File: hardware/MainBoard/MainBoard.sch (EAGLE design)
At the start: 220 parts, among them J1 CON-71741-2184-BOT, J2 CON-71741-2184-TOP, J3 CON-FTSH-105-01-L-DV-K, J4 CON-ZX62R-B-5P, J5 CON-SMA, J6 CON-SMA, J7 CON-RJ45-J0G-0007NL, J8 SWITCH-CJS-1200-1200, M1 MOUNT-HOLE3.3, M2 MOUNT-HOLE3.3, M3 MOUNT-HOLE3.3, M4 MOUNT-HOLE3.3, M5 FIDUCIAL1X2, M6 FIDUCIAL1X2, M7 FIDUCIAL1X2, M8 FIDUCIAL1X2, Q1 MMBT3904, SW1 SWITCH-KSC-201J, SW2 SWITCH-KSC-201J, U1 A2F500M3G-FG256, U2 MAX19706-T4877-4, U3 MAX19706-T4877-4, U4 USBLC6-2SC6, U5 FT232HL, U6 DP83848C-VBH48A, U7 93LC56BT-OT, U8 DS1818-10-SOT-23, U9 LMV112, X1 FOX924B, X2 ECX-31B, X3 ASEM1-C, X5 ECX-42-120

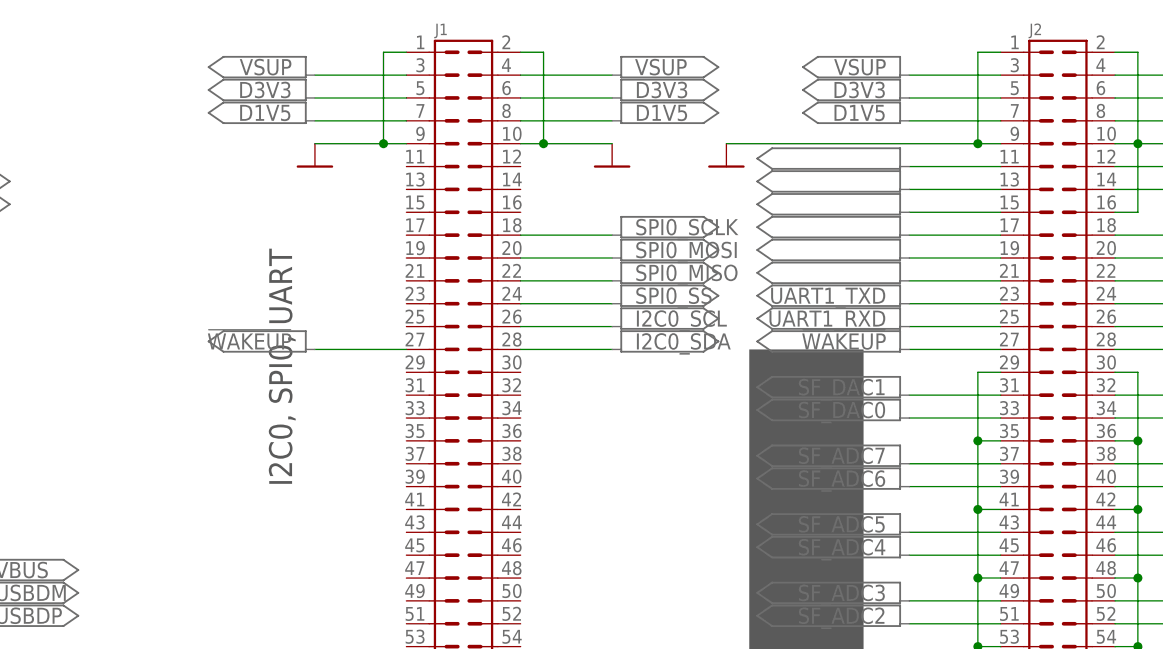
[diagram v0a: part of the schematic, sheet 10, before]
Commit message: Minor updates on the connector on the schematic.
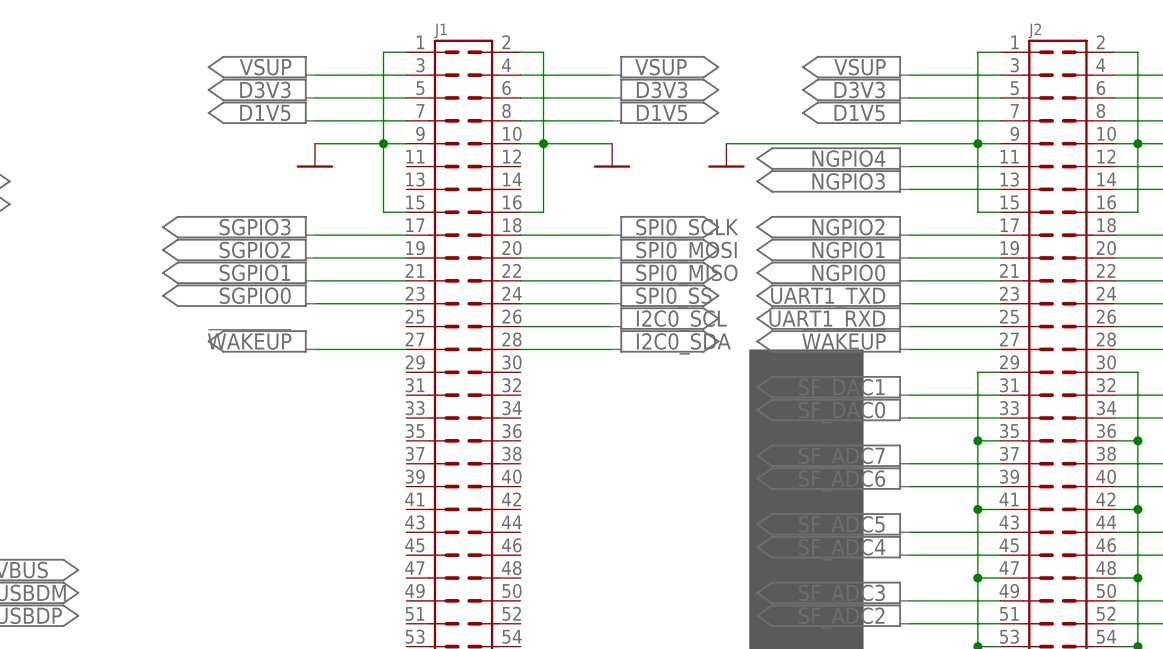
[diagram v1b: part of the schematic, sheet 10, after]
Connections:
- net N$10 renamed NGPIO4
- net N$2 renamed NGPIO3
- net N$3 renamed NGPIO0
- net N$5 renamed NGPIO1
- net N$7 renamed NGPIO2
- removed net N$1: J2.15
- new net SGPIO0: J1.23
- new net SGPIO1: J1.21
- new net SGPIO2: J1.19
- new net SGPIO3: J1.17
- net DGND: now also J1.15, J1.16, J2.15
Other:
- note added: "Make it a differential FPGAIO"
- note removed: "I2C0, SPI0, UART"
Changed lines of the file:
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@@
 <setting verticaltext="up"/>
 </settings>
-<grid distance="0.1" unitdist="inch" unit="inch" style="lines" multiple="1" display="no" altdistance="0.01" altunitdist="inch" altunit="inch"/>
+<grid distance="0.1" unitdist="inch" unit="inch" style="lines" multiple="1" display="no" altdistance="0.05" altunitdist="inch" altunit="inch"/>
 <layers>
 <layer number="1" name="Top" color="4" fill="1" visible="no" active="no"/>
@@
 <layer number="113" name="Route13" color="7" fill="1" visible="no" active="no"/>
 <layer number="114" name="FIXED_SF_PIN" color="2" fill="3" visible="yes" active="yes"/>
-<layer number="116" name="Patch_BOT" color="9" fill="4" visible="yes" active="yes"/>
+<layer number="116" name="Patch_BOT" color="9" fill="4" visible="no" active="yes"/>
 <layer number="117" name="mPads" color="7" fill="1" visible="no" active="no"/>
 <layer number="118" name="mVias" color="7" fill="1" visible="no" active="no"/>
@@
 <part name="PORT350" library="MainBoard" deviceset="PORT7" device=""/>
 <part name="U$20" library="MainBoard" deviceset="DGND" device=""/>
+<part name="PORT323" library="MainBoard" deviceset="PORT7" device=""/>
+<part name="PORT351" library="MainBoard" deviceset="PORT7" device=""/>
+<part name="PORT352" library="MainBoard" deviceset="PORT7" device=""/>
 </parts>
 <sheets>
@@
 <text x="64.77" y="149.86" size="1.778" layer="97">NC</text>
 <text x="45.72" y="76.2" size="50.8" layer="208">CON</text>
-<text x="116.84" y="114.3" size="2.54" layer="97" rot="R90">I2C0, SPI0, UART</text>
-<rectangle x1="167.64" y1="137.16" x2="187.96" y2="151.13" layer="98"/>
+<rectangle x1="170.18" y1="147.32" x2="187.96" y2="152.4" layer="98"/>
+<text x="172.72" y="149.86" size="1.778" layer="98" rot="R90">Make it a differential FPGAIO</text>
 </plain>
 <instances>
@@
 <instance part="PORT346" gate="G$1" x="170.18" y="139.7" rot="MR0"/>
 <instance part="PORT347" gate="G$1" x="170.18" y="142.24" rot="MR0"/>
-<instance part="PORT348" gate="G$1" x="170.18" y="144.78" rot="MR0"/>
+<instance part="PORT348" gate="G$1" x="104.14" y="142.24" rot="MR0"/>
 <instance part="PORT349" gate="G$1" x="170.18" y="147.32" rot="MR0"/>
 <instance part="PORT350" gate="G$1" x="170.18" y="149.86" rot="MR0"/>
+<instance part="PORT323" gate="G$1" x="104.14" y="134.62" rot="MR0"/>
+<instance part="PORT351" gate="G$1" x="104.14" y="137.16" rot="MR0"/>
+<instance part="PORT352" gate="G$1" x="104.14" y="139.7" rot="MR0"/>
 </instances>
 <busses>
@@
 <wire x1="127" y1="152.4" x2="129.54" y2="152.4" width="0.1524" layer="91"/>
 <junction x="127" y="152.4"/>
+<wire x1="127" y1="152.4" x2="127" y2="144.78" width="0.1524" layer="91"/>
+<pinref part="J1" gate="G$1" pin="15"/>
+<wire x1="127" y1="144.78" x2="129.54" y2="144.78" width="0.1524" layer="91"/>
 </segment>
 <segment>
@@
 <wire x1="142.24" y1="152.4" x2="144.78" y2="152.4" width="0.1524" layer="91"/>
 <junction x="144.78" y="152.4"/>
+<pinref part="J1" gate="G$1" pin="16"/>
+<wire x1="142.24" y1="144.78" x2="144.78" y2="144.78" width="0.1524" layer="91"/>
+<wire x1="144.78" y1="144.78" x2="144.78" y2="152.4" width="0.1524" layer="91"/>
 </segment>
 <segment>
@@
 <wire x1="193.04" y1="162.56" x2="195.58" y2="162.56" width="0.1524" layer="91"/>
 <junction x="193.04" y="152.4"/>
+<pinref part="J2" gate="G$1" pin="15"/>
+<wire x1="195.58" y1="144.78" x2="193.04" y2="144.78" width="0.1524" layer="91"/>
+<wire x1="193.04" y1="144.78" x2="193.04" y2="152.4" width="0.1524" layer="91"/>
 </segment>
 <segment>
@@
 </segment>
 </net>
-<net name="N$3" class="0">
+<net name="NGPIO0" class="0">
 <segment>
 <pinref part="J2" gate="G$1" pin="21"/>
 <wire x1="195.58" y1="137.16" x2="185.42" y2="137.16" width="0.1524" layer="91"/>
+<label x="182.88" y="137.16" size="1.778" layer="95" rot="MR0"/>
 </segment>
 </net>
-<net name="N$5" class="0">
+<net name="NGPIO1" class="0">
 <segment>
 <pinref part="J2" gate="G$1" pin="19"/>
 <wire x1="195.58" y1="139.7" x2="185.42" y2="139.7" width="0.1524" layer="91"/>
+<label x="182.88" y="139.7" size="1.778" layer="95" rot="MR0"/>
 </segment>
 </net>
-<net name="N$7" class="0">
+<net name="NGPIO2" class="0">
 <segment>
 <pinref part="J2" gate="G$1" pin="17"/>
 <wire x1="195.58" y1="142.24" x2="185.42" y2="142.24" width="0.1524" layer="91"/>
+<label x="182.88" y="142.24" size="1.778" layer="95" rot="MR0"/>
 </segment>
 </net>
-<net name="N$1" class="0">
+<net name="SGPIO3" class="0">
 <segment>
-<pinref part="J2" gate="G$1" pin="15"/>
-<wire x1="195.58" y1="144.78" x2="185.42" y2="144.78" width="0.1524" layer="91"/>
+<wire x1="129.54" y1="142.24" x2="119.38" y2="142.24" width="0.1524" layer="91"/>
+<label x="116.84" y="142.24" size="1.778" layer="95" rot="MR0"/>
+<pinref part="J1" gate="G$1" pin="17"/>
 </segment>
 </net>
-<net name="N$2" class="0">
+<net name="NGPIO3" class="0">
 <segment>
 <pinref part="J2" gate="G$1" pin="13"/>
 <wire x1="195.58" y1="147.32" x2="185.42" y2="147.32" width="0.1524" layer="91"/>
+<label x="182.88" y="147.32" size="1.778" layer="95" rot="MR0"/>
 </segment>
 </net>
-<net name="N$10" class="0">
+<net name="NGPIO4" class="0">
 <segment>
 <pinref part="J2" gate="G$1" pin="11"/>
 <wire x1="195.58" y1="149.86" x2="185.42" y2="149.86" width="0.1524" layer="91"/>
+<label x="182.88" y="149.86" size="1.778" layer="95" rot="MR0"/>
 </segment>
 </net>
@@
 </segment>
 </net>
+<net name="SGPIO0" class="0">
+<segment>
+<pinref part="J1" gate="G$1" pin="23"/>
+<wire x1="129.54" y1="134.62" x2="119.38" y2="134.62" width="0.1524" layer="91"/>
+<label x="116.84" y="134.62" size="1.778" layer="95" rot="MR0"/>
+</segment>
+</net>
+<net name="SGPIO1" class="0">
+<segment>
+<pinref part="J1" gate="G$1" pin="21"/>
+<wire x1="129.54" y1="137.16" x2="119.38" y2="137.16" width="0.1524" layer="91"/>
+<label x="116.84" y="137.16" size="1.778" layer="95" rot="MR0"/>
+</segment>
+</net>
+<net name="SGPIO2" class="0">
+<segment>
+<pinref part="J1" gate="G$1" pin="19"/>
+<wire x1="129.54" y1="139.7" x2="119.38" y2="139.7" width="0.1524" layer="91"/>
+<label x="116.84" y="139.7" size="1.778" layer="95" rot="MR0"/>
+</segment>
+</net>

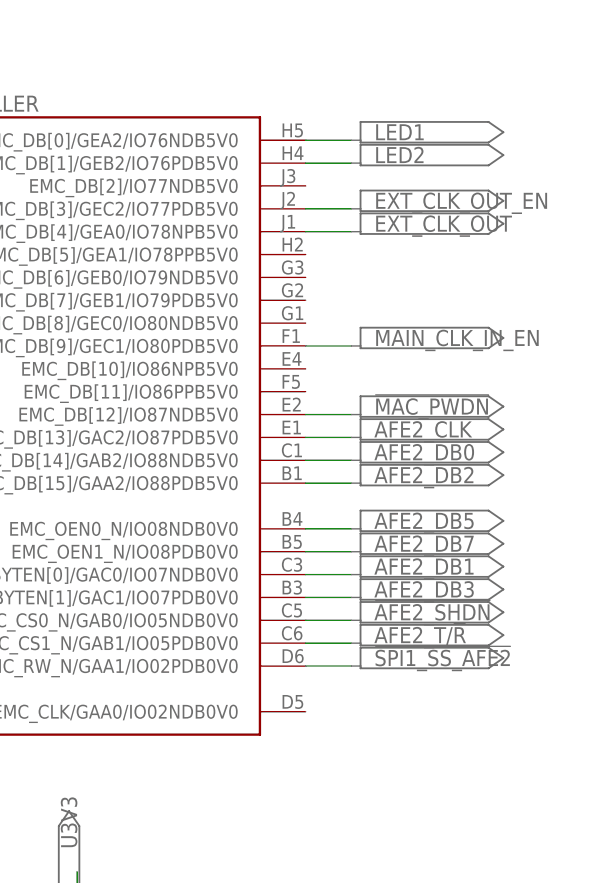
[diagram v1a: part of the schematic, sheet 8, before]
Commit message: 
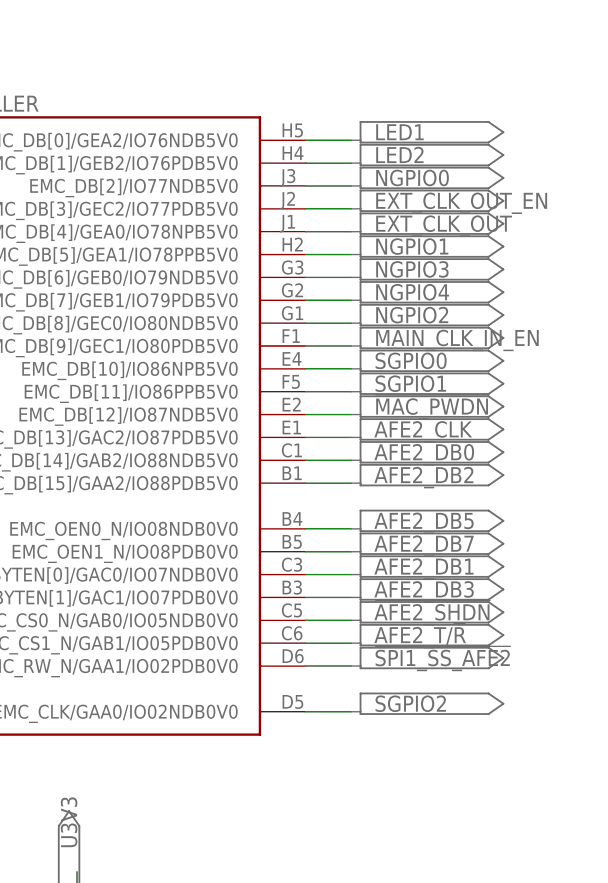
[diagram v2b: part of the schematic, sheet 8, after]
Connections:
- removed net N$6: U1-IOB.IO84NDB5V0
- net NGPIO0: now also U1-EXTERNAL-MEMORY-CONTROLLER.EMC_DB[2]/IO77NDB5V0
- net NGPIO1: now also U1-EXTERNAL-MEMORY-CONTROLLER.EMC_DB[5]/GEA1/IO78PPB5V0
- net NGPIO2: now also U1-EXTERNAL-MEMORY-CONTROLLER.EMC_DB[8]/GEC0/IO80NDB5V0
- net NGPIO3: now also U1-EXTERNAL-MEMORY-CONTROLLER.EMC_DB[6]/GEB0/IO79NDB5V0
- net NGPIO4: now also U1-EXTERNAL-MEMORY-CONTROLLER.EMC_DB[7]/GEB1/IO79PDB5V0
- net SGPIO0: now also U1-EXTERNAL-MEMORY-CONTROLLER.EMC_DB[10]/IO86NPB5V0
- net SGPIO1: now also U1-EXTERNAL-MEMORY-CONTROLLER.EMC_DB[11]/IO86PPB5V0
- net SGPIO2: now also U1-EXTERNAL-MEMORY-CONTROLLER.EMC_CLK/GAA0/IO02NDB0V0
- net SGPIO3: now also U1-IOB.IO84NDB5V0
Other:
- note added: "Make it a differential GCL IN"
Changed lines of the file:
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@@
 <layer number="113" name="Route13" color="7" fill="1" visible="no" active="no"/>
 <layer number="114" name="FIXED_SF_PIN" color="2" fill="3" visible="yes" active="yes"/>
-<layer number="116" name="Patch_BOT" color="9" fill="4" visible="no" active="yes"/>
+<layer number="116" name="Patch_BOT" color="9" fill="4" visible="yes" active="yes"/>
 <layer number="117" name="mPads" color="7" fill="1" visible="no" active="no"/>
 <layer number="118" name="mVias" color="7" fill="1" visible="no" active="no"/>
@@
 <part name="PORT351" library="MainBoard" deviceset="PORT7" device=""/>
 <part name="PORT352" library="MainBoard" deviceset="PORT7" device=""/>
+<part name="PORT353" library="MainBoard" deviceset="PORT7" device=""/>
+<part name="PORT354" library="MainBoard" deviceset="PORT7" device=""/>
+<part name="PORT355" library="MainBoard" deviceset="PORT7" device=""/>
+<part name="PORT356" library="MainBoard" deviceset="PORT7" device=""/>
+<part name="PORT357" library="MainBoard" deviceset="PORT7" device=""/>
+<part name="PORT358" library="MainBoard" deviceset="PORT7" device=""/>
+<part name="PORT359" library="MainBoard" deviceset="PORT7" device=""/>
+<part name="PORT360" library="MainBoard" deviceset="PORT7" device=""/>
 </parts>
 <sheets>
@@
 <plain>
 <text x="198.12" y="20.32" size="5.08" layer="97">USB</text>
-<rectangle x1="218.44" y1="86.36" x2="238.76" y2="99.06" layer="98"/>
 <rectangle x1="114.3" y1="88.9" x2="134.62" y2="96.52" layer="98"/>
 <text x="167.64" y="38.1" size="2.54" layer="97">EEPROM</text>
@@
 <rectangle x1="109.22" y1="111.76" x2="116.84" y2="116.84" layer="101"/>
 <rectangle x1="76.2" y1="109.22" x2="104.14" y2="160.02" layer="116"/>
+<rectangle x1="218.44" y1="149.86" x2="238.76" y2="151.13" layer="116"/>
+<rectangle x1="218.44" y1="134.62" x2="238.76" y2="144.78" layer="116"/>
+<rectangle x1="220.98" y1="127" x2="238.76" y2="132.08" layer="116"/>
+<rectangle x1="218.44" y1="91.44" x2="238.76" y2="93.98" layer="116"/>
 </plain>
 <instances>
@@
 <instance part="PORT299" gate="G$1" x="236.22" y="144.78"/>
 <instance part="PORT300" gate="G$1" x="236.22" y="147.32"/>
+<instance part="PORT353" gate="G$1" x="236.22" y="142.24"/>
+<instance part="PORT354" gate="G$1" x="236.22" y="139.7"/>
+<instance part="PORT355" gate="G$1" x="236.22" y="149.86"/>
+<instance part="PORT356" gate="G$1" x="236.22" y="137.16"/>
+<instance part="PORT357" gate="G$1" x="236.22" y="134.62"/>
+<instance part="PORT358" gate="G$1" x="236.22" y="129.54"/>
+<instance part="PORT359" gate="G$1" x="236.22" y="127"/>
+<instance part="PORT360" gate="G$1" x="236.22" y="91.44"/>
 </instances>
 <busses>
@@
 </segment>
 </net>
+<net name="NGPIO0" class="0">
+<segment>
+<pinref part="U1" gate="-EXTERNAL-MEMORY-CONTROLLER" pin="EMC_DB[2]/IO77NDB5V0"/>
+<wire x1="215.9" y1="149.86" x2="220.98" y2="149.86" width="0.1524" layer="91"/>
+<label x="223.52" y="149.86" size="1.778" layer="95"/>
+</segment>
+</net>
+<net name="NGPIO1" class="0">
+<segment>
+<pinref part="U1" gate="-EXTERNAL-MEMORY-CONTROLLER" pin="EMC_DB[5]/GEA1/IO78PPB5V0"/>
+<wire x1="215.9" y1="142.24" x2="220.98" y2="142.24" width="0.1524" layer="91"/>
+<label x="223.52" y="142.24" size="1.778" layer="95"/>
+</segment>
+</net>
+<net name="NGPIO3" class="0">
+<segment>
+<pinref part="U1" gate="-EXTERNAL-MEMORY-CONTROLLER" pin="EMC_DB[6]/GEB0/IO79NDB5V0"/>
+<wire x1="215.9" y1="139.7" x2="220.98" y2="139.7" width="0.1524" layer="91"/>
+<label x="223.52" y="139.7" size="1.778" layer="95"/>
+</segment>
+</net>
+<net name="NGPIO4" class="0">
+<segment>
+<pinref part="U1" gate="-EXTERNAL-MEMORY-CONTROLLER" pin="EMC_DB[7]/GEB1/IO79PDB5V0"/>
+<wire x1="215.9" y1="137.16" x2="220.98" y2="137.16" width="0.1524" layer="91"/>
+<label x="223.52" y="137.16" size="1.778" layer="95"/>
+</segment>
+</net>
+<net name="SGPIO0" class="0">
+<segment>
+<pinref part="U1" gate="-EXTERNAL-MEMORY-CONTROLLER" pin="EMC_DB[10]/IO86NPB5V0"/>
+<wire x1="215.9" y1="129.54" x2="220.98" y2="129.54" width="0.1524" layer="91"/>
+<label x="223.52" y="129.54" size="1.778" layer="95"/>
+</segment>
+</net>
+<net name="SGPIO1" class="0">
+<segment>
+<pinref part="U1" gate="-EXTERNAL-MEMORY-CONTROLLER" pin="EMC_DB[11]/IO86PPB5V0"/>
+<wire x1="215.9" y1="127" x2="220.98" y2="127" width="0.1524" layer="91"/>
+<label x="223.52" y="127" size="1.778" layer="95"/>
+</segment>
+</net>
+<net name="NGPIO2" class="0">
+<segment>
+<pinref part="U1" gate="-EXTERNAL-MEMORY-CONTROLLER" pin="EMC_DB[8]/GEC0/IO80NDB5V0"/>
+<wire x1="215.9" y1="134.62" x2="220.98" y2="134.62" width="0.1524" layer="91"/>
+<label x="223.52" y="134.62" size="1.778" layer="95"/>
+</segment>
+</net>
+<net name="SGPIO2" class="0">
+<segment>
+<pinref part="U1" gate="-EXTERNAL-MEMORY-CONTROLLER" pin="EMC_CLK/GAA0/IO02NDB0V0"/>
+<wire x1="215.9" y1="91.44" x2="220.98" y2="91.44" width="0.1524" layer="91"/>
+<label x="223.52" y="91.44" size="1.778" layer="95"/>
+</segment>
+</net>
 </nets>
 </sheet>
@@
 <rectangle x1="215.9" y1="83.82" x2="233.68" y2="88.9" layer="101"/>
 <rectangle x1="215.9" y1="68.58" x2="223.52" y2="73.66" layer="98"/>
+<rectangle x1="203.2" y1="71.12" x2="233.68" y2="73.66" layer="116"/>
 </plain>
 <instances>
@@
 </segment>
 </net>
-<net name="N$6" class="0">
+<net name="SGPIO3" class="0">
 <segment>
 <pinref part="U1" gate="-IOB" pin="IO84NDB5V0"/>
@@
 <rectangle x1="170.18" y1="147.32" x2="187.96" y2="152.4" layer="98"/>
 <text x="172.72" y="149.86" size="1.778" layer="98" rot="R90">Make it a differential FPGAIO</text>
+<text x="170.18" y="149.86" size="1.778" layer="98" rot="R90">Make it a differential GCL IN</text>
+<text x="233.68" y="149.86" size="1.778" layer="98" rot="R90">Make it a differential GCL IN</text>
 </plain>
 <instances>
